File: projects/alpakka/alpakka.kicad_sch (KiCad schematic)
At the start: 65 parts, among them P1 Conn_01x20_Pin, P2 Conn_01x20_Pin, P3 Headers 4P IN, P4 Blade, P5 Jack 2.5mm, P6 Conn_01x02, U1 Alpsalpine_RKJXV, U10 ST_LSM6, U12 ST_LSM6, U2 Alpsalpine_RKJXV, U3 Alpsalpine_EC10E, U6 NXP_PCAL6416A, U8 NXP_PCAL6416A

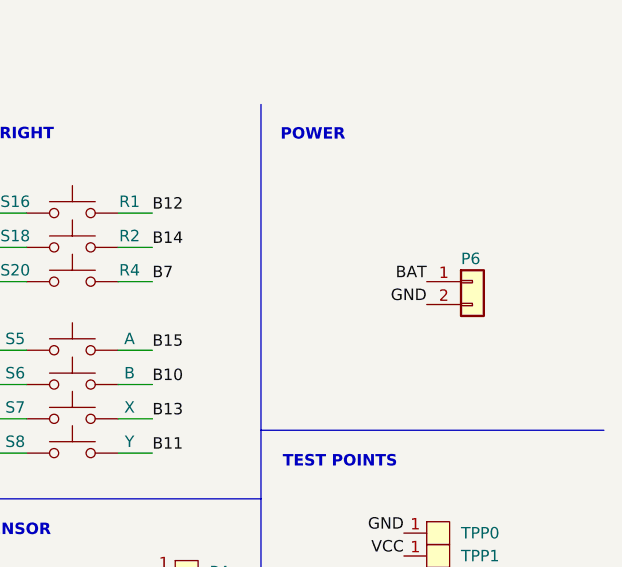
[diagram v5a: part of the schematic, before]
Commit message: Battery connector silk placement and 3D model
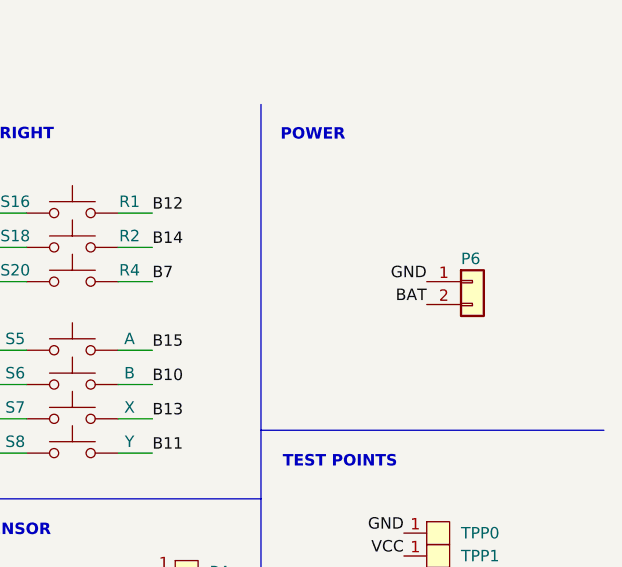
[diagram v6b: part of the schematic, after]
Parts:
- P6: Export (none) -> yes; LCSC (none) -> C5359610; Mount (none) -> TH
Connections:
- net BAT: now also P6.2 (Pin_2); no longer P6.1 (Pin_1)
- net GND: now also P6.1 (Pin_1); no longer P6.2 (Pin_2)
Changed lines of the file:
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@@
 		)
 	)
-	(label "BAT"
+	(label "GND"
 		(at 208.28 31.75 180)
 		(fields_autoplaced yes)
@@
 		)
 	)
-	(label "GND"
+	(label "BAT"
 		(at 208.28 34.29 180)
 		(fields_autoplaced yes)
@@
 			)
 		)
-		(property "Mount" ""
+		(property "Mount" "TH"
 			(at 213.36 31.75 0)
 			(effects
@@
 			)
 		)
-		(property "Export" ""
+		(property "Export" "yes"
 			(at 213.36 31.75 0)
 			(effects
@@
 			(at 213.36 31.75 0)
 			(effects
+				(font
+					(size 1.27 1.27)
+				)
+				(hide yes)
+			)
+		)
+		(property "LCSC" "C5359610"
+			(at 213.36 31.75 0)
+			(effects

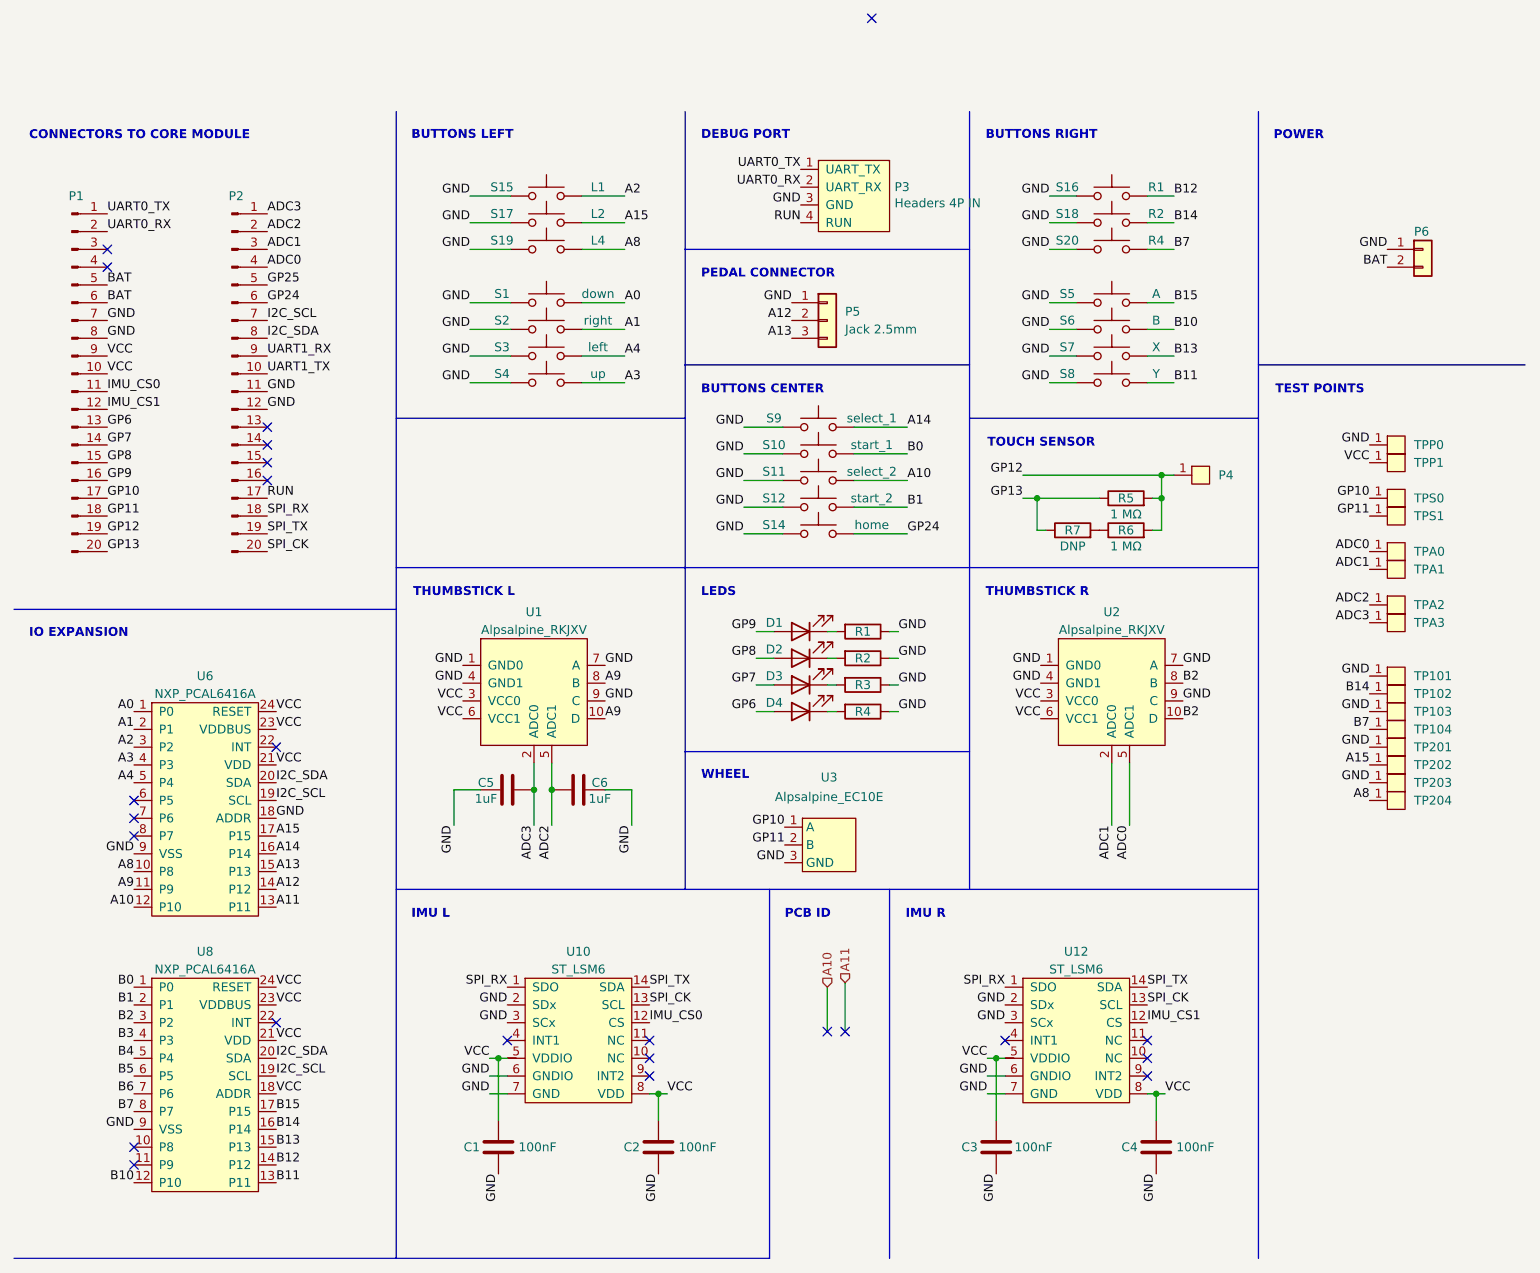
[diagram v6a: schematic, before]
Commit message: Thumbsticks without far caps, Thumbstick test points, Scrollwheel support dedicated holes
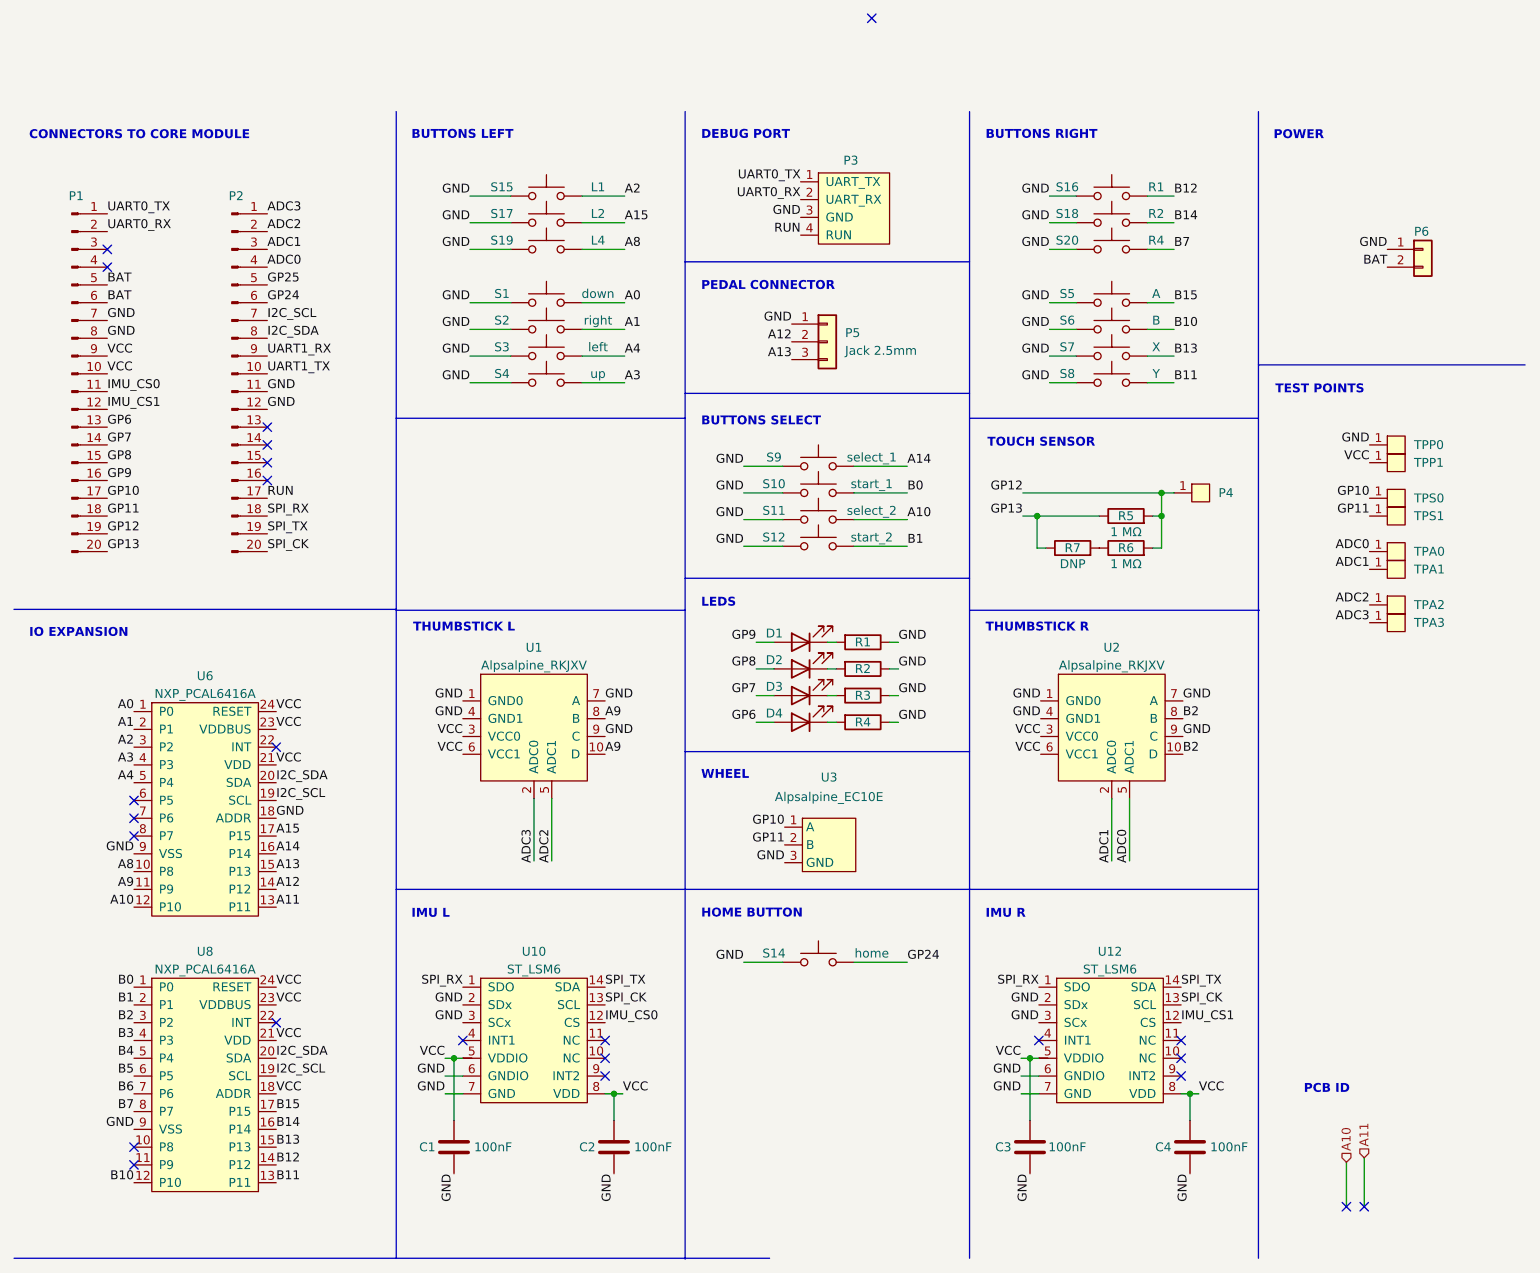
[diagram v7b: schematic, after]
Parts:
- removed C5, C6: 1uF, ILO_fp:0402, symbol Device:C
- removed TP101, TP102, TP103, TP104, TP201, TP202, TP203, TP204: Endpoint, ILO_fp:Pad_1mm, symbol ILO_sym:Endpoint
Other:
- note added: "BUTTONS SELECT"
- note added: "HOME BUTTON"
- note removed: "BUTTONS CENTER"
- moved on the sheet: C1, C2, C3, C4, D1, D2, D3, D4, P3, P4, P5, R1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

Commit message: Added battery test point, Layout tweaks
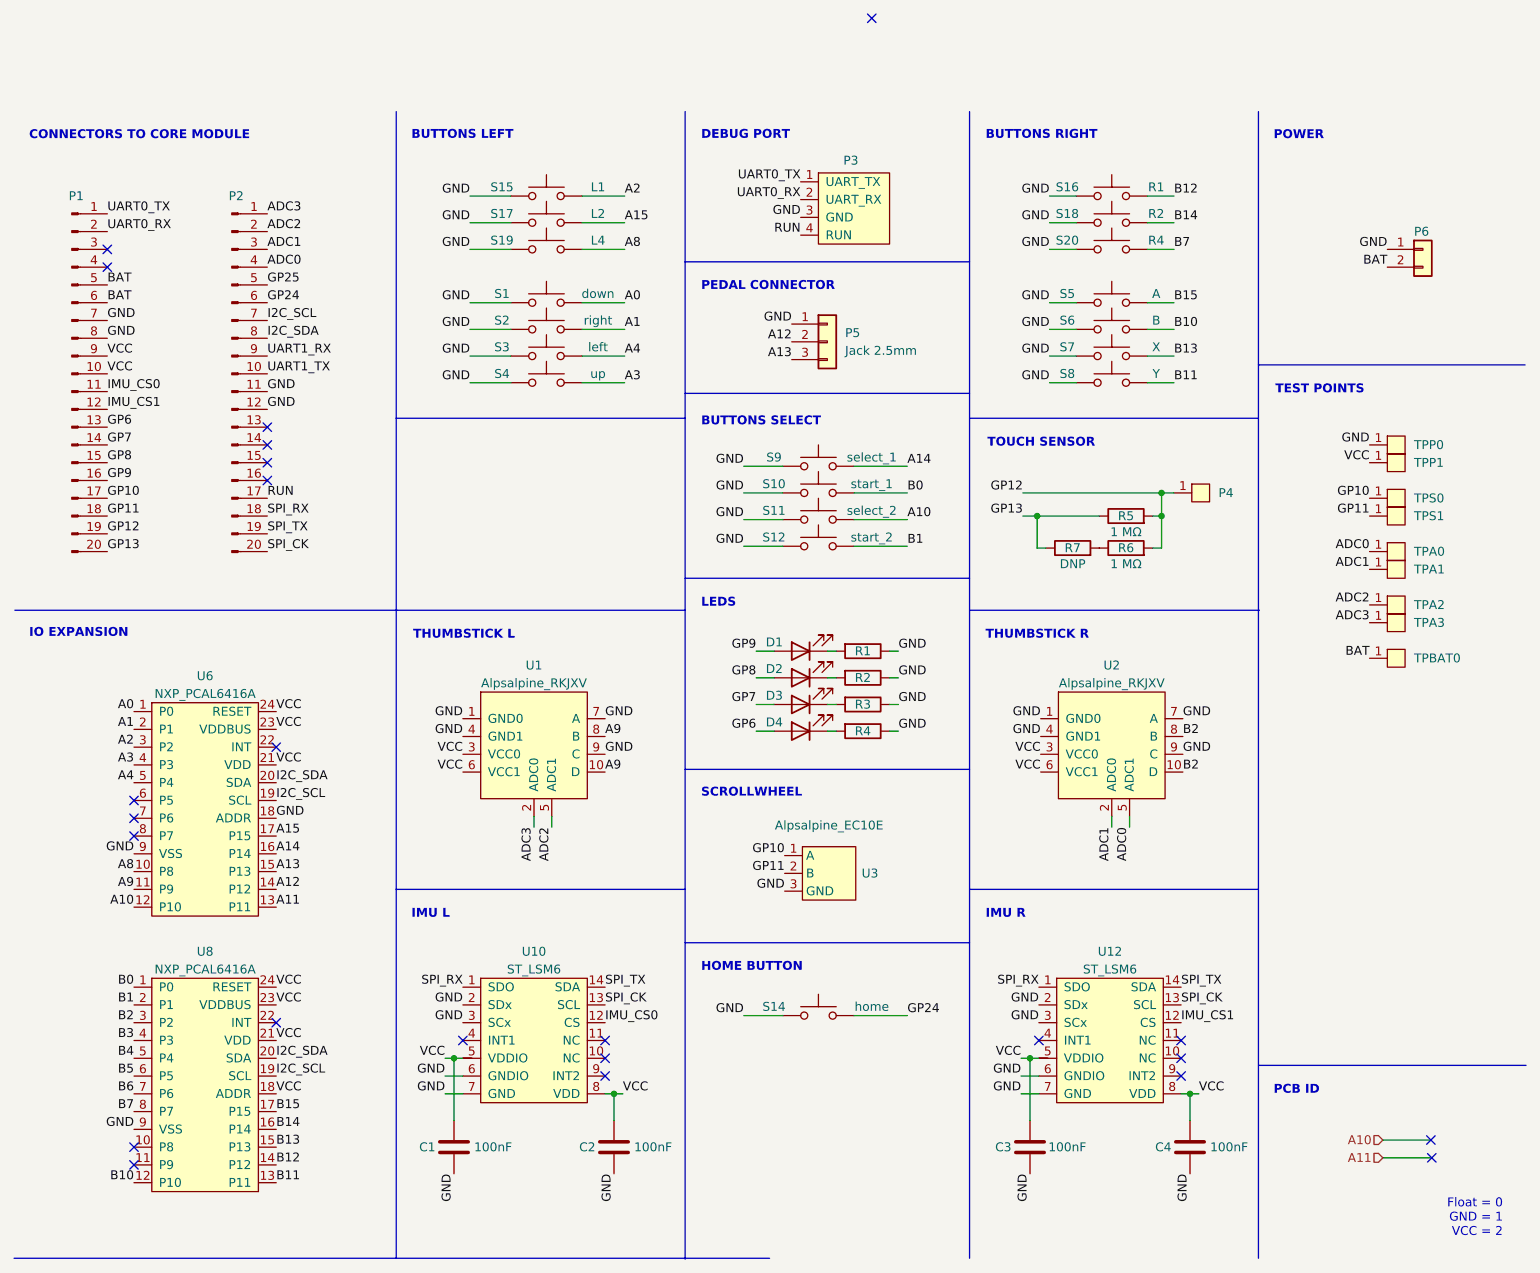
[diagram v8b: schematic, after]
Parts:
- added TPBAT0: Endpoint, ILO_fp:Pad_1mm, symbol ILO_sym:Endpoint
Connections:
- net BAT: now also TPBAT0.1
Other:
- note added: "Float = 0 GND = 1 VCC = 2"
- note added: "SCROLLWHEEL"
- note removed: "WHEEL"
- moved on the sheet: D1, D2, D3, D4, R1, R2, R3, R4, S14, U1, U2, U3
